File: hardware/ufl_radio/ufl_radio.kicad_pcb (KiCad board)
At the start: 6 copper layers, 46.8 x 62 mm, 142 parts, among them J2 U.FL, J3 Shield, J4 Shield, J5 U.FL, J6 Shield, J7 U.FL, J8 Shield, J9 U.FL, U1 MAX2769B, U2 CS48520S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

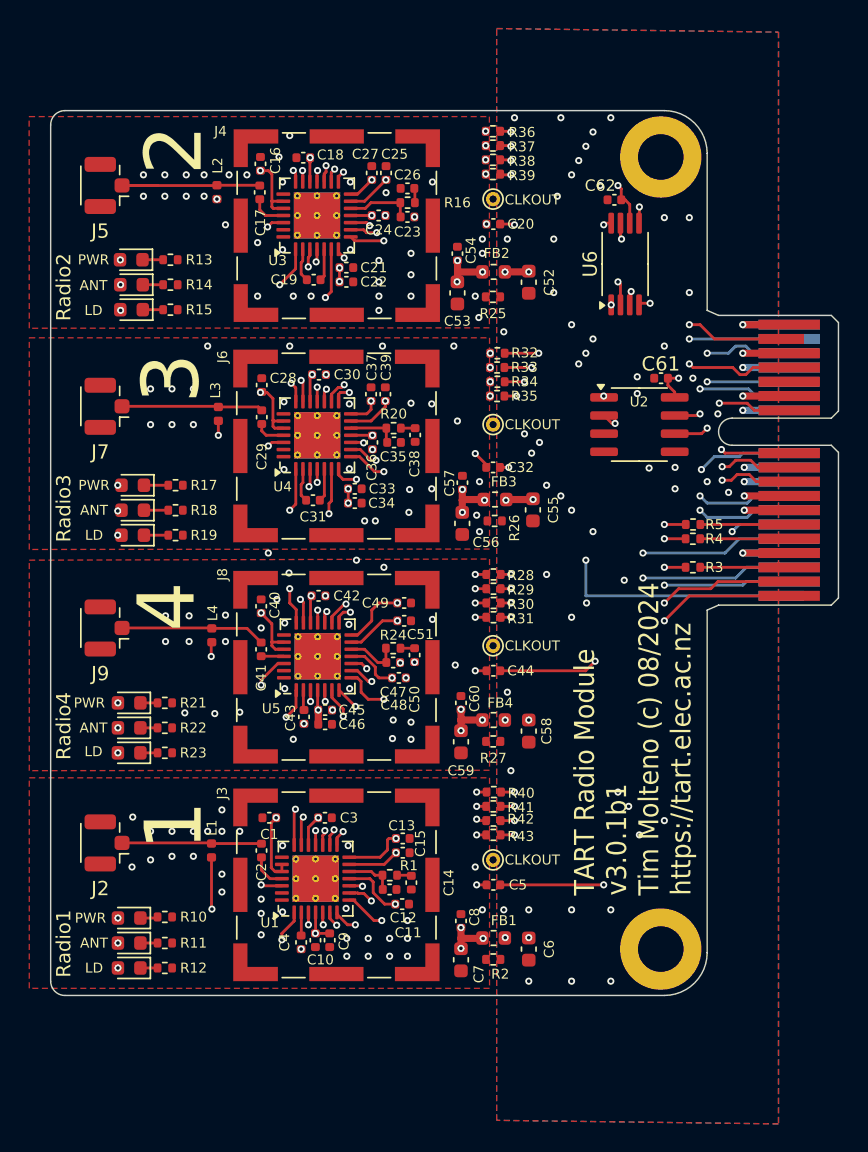
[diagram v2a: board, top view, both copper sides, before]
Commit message: Updated the order of radios
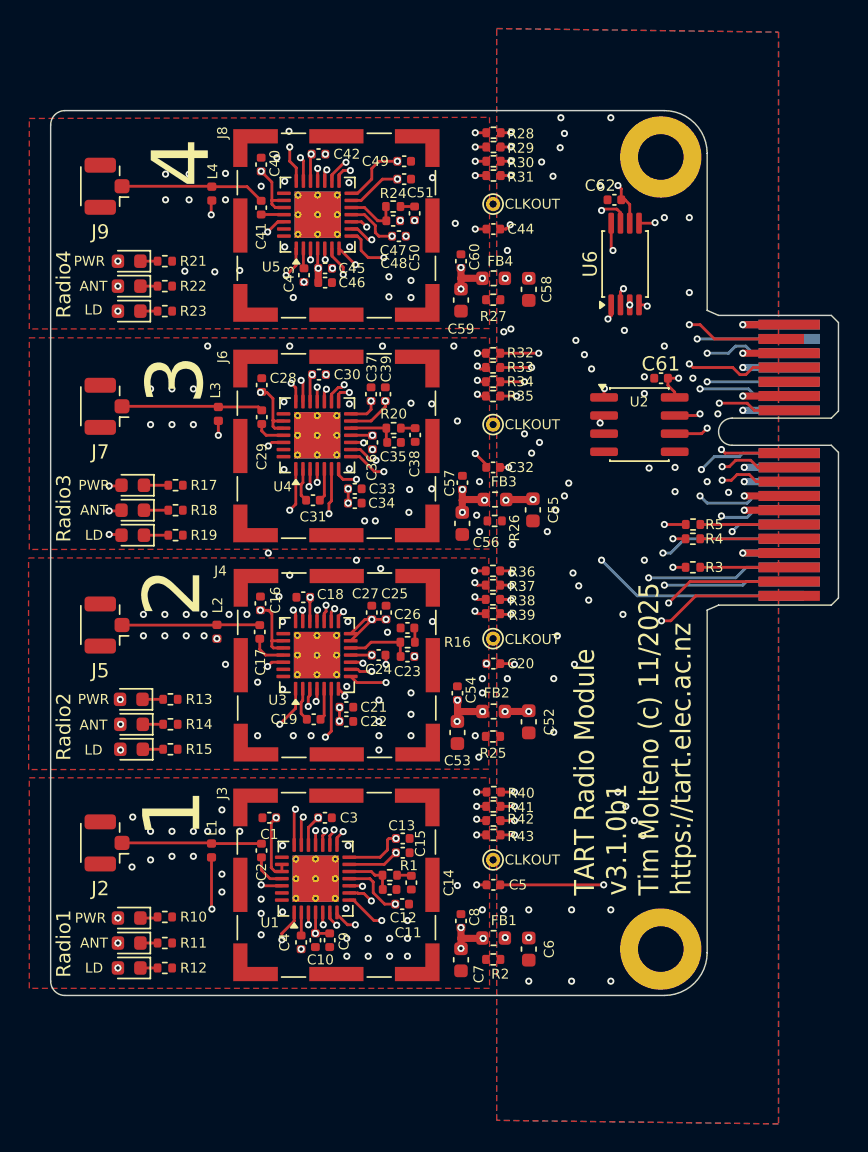
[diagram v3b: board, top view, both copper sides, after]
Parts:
- moved C40 31.0 mm to (174.8, 77.8)
- moved C41 31.0 mm to (174.8, 80.8)
- moved C42 31.0 mm to (178.8, 77.0)
- moved C43 31.0 mm to (177.8, 85.5)
- moved C44 31.0 mm to (191.0, 82.3)
- moved C45 31.0 mm to (179.2, 85.0)
- moved C46 31.0 mm to (179.2, 86.0)
- moved C47 31.0 mm to (184.0, 81.7)
- moved C48 31.0 mm to (184.4, 82.8)
- moved C49 31.0 mm to (184.8, 77.5)
- moved C50 31.0 mm to (185.5, 81.2)
- moved C51 31.0 mm to (184.8, 78.8)
- moved C60 31.0 mm to (188.8, 84.5)
- moved D10 31.0 mm to (165.5, 84.5)
- moved D11 31.0 mm to (165.5, 86.3)
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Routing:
- net CLKIN_2: track 7.84 -> 37.5 mm, vias 2 -> 3
- net CLKIN_4: track 38.7 -> 9.85 mm
- net R4_Q0: track 25.2 -> 46.1 mm
- net R4_I0: track 26.7 -> 45.0 mm, vias 3 -> 4
- net R4_I1: track 27.4 -> 45.4 mm
- net R4_Q1: track 28.1 -> 43.9 mm
- net R2_Q1: track 30.6 -> 40.1 mm
- net Net-(J5-In): track 12.2 -> 9.67 mm
- net R2_Q0: track 35.0 -> 37.0 mm
- net R2_I1: track 34.8 -> 36.5 mm
- net CLKIN_1: track 50.6 -> 49.0 mm
- net CLKIN_3: track 30.7 -> 29.1 mm
- net R2_I0: track 35.2 -> 36.7 mm
- net /Radio3/LD: track 18.6 -> 20.1 mm
- net /Radio3/ANTFLAG: track 15.1 -> 16.6 mm
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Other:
- board text added: "TART Radio Module v3.1.0b1 Tim Molteno (c) 11/2025 https://tart.elec.ac.nz"
- board text added: "TART Radio Telescope Radio Module v3.1.0b1 Tim Molteno (c) 11/2025 https://tart.elec.ac.nz"
- board text removed: "TART Radio Module v3.0.1b1 Tim Molteno (c) 08/2024 https://tart.elec.ac.nz"
- board text removed: "TART Radio Telescope Radio Module v3.0.1b1 Tim Molteno (c) 08/2024 https://tart.elec.ac.nz"

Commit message: Minor updates
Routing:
- net GNDREF: track 30.4 -> 29.8 mm
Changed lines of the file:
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@@
-	)
-	(segment
-		(start 198.775 95.365)
-		(end 198.5 95.64)
-		(width 0.2)
-		(layer "F.Cu")
-		(net 27)
 	)
 	(segment
@@
 		(end 211.75 89)
 		(width 0.5)
-		(layer "F.Cu")
-		(net 27)
-	)
-	(segment
-		(start 198.5 95.64)
-		(end 198.5 95.887475)
-		(width 0.2)
 		(layer "F.Cu")
 		(net 27)
@@
 	)
 	(via
-		(at 198.5 95.887475)
-		(size 0.5)
-		(drill 0.25)
+		(at 201.7 95.5)
+		(size 0.5)
+		(drill 0.25)

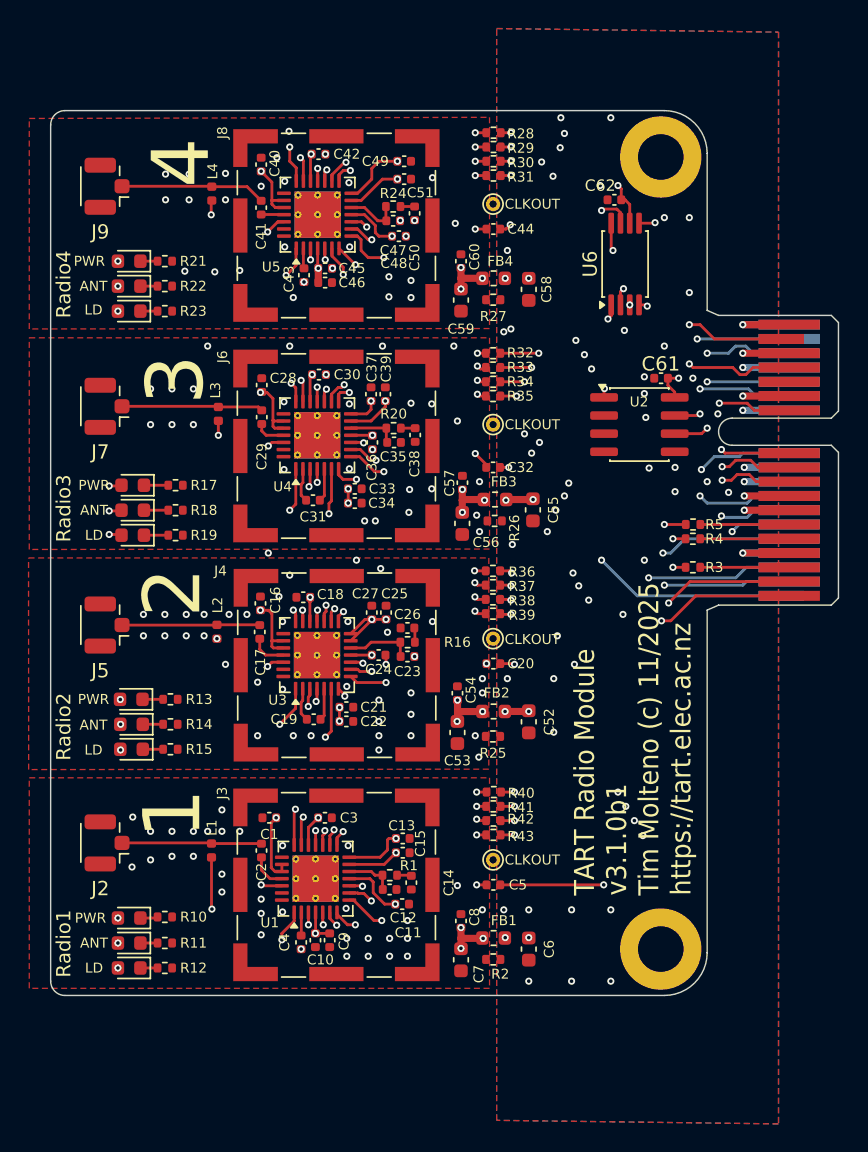
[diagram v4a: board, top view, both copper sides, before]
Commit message: Added radio board with identical sections
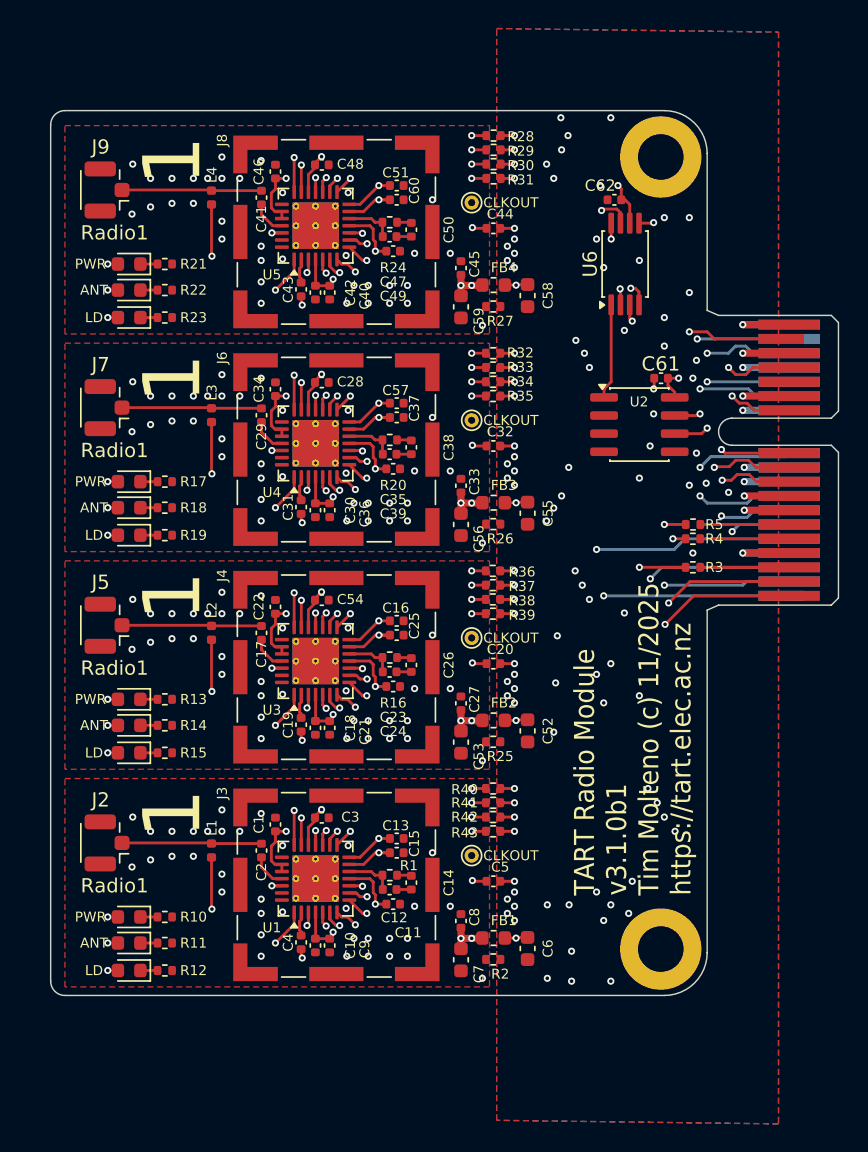
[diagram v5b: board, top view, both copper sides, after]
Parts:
- moved C54 11.5 mm to (179.0, 108.3), turned to 0 degrees
- moved C40 10.2 mm to (179.6, 86.8), turned to -90 degrees
- moved C34 9.73 mm to (175.8, 93.5), turned to 90 degrees
- moved C42 9.70 mm to (178.6, 86.8), turned to -90 degrees
- moved C16 9.63 mm to (184.2, 109.8), turned to 0 degrees
- moved C45 9.52 mm to (188.8, 85.0), turned to 90 degrees
- moved C30 9.50 mm to (178.6, 102.0), turned to -90 degrees
- moved C22 9.44 mm to (175.8, 108.8), turned to 90 degrees
- moved C18 9.19 mm to (178.6, 117.2), turned to -90 degrees
- moved C27 8.92 mm to (188.8, 115.5)
- moved C46 8.52 mm to (175.8, 78.3), turned to 90 degrees
- moved C33 7.44 mm to (188.8, 100.3), turned to 90 degrees
- moved C48 7.36 mm to (179.0, 77.8)
- moved C57 7.22 mm to (184.2, 94.5), turned to 0 degrees
- moved C49 6.35 mm to (184.0, 83.8)
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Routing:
- net PGM: track 88.3 -> 156.0 mm, vias 6 -> 12
- net /SHDN: track 84.0 -> 134.9 mm, vias 6 -> 12
- net SDATA: track 81.9 -> 131.4 mm, vias 6 -> 13
- net SCLK: track 76.9 -> 49.6 mm, vias 6 -> 9
- net CS#: track 73.6 -> 46.7 mm, vias 6 -> 9
- net R3_I0: track 27.4 -> 6.06 mm, vias 3 -> 2
- net R3_I1: track 27.6 -> 6.65 mm, vias 3 -> 2
- net R3_Q0: track 24.4 -> 5.84 mm, vias 3 -> 2
- net /Radio2/3v3_local: track 18.1 -> 25.8 mm, vias 12 -> 9
- net /Radio3/3v3_local: track 19.3 -> 25.8 mm, vias 12 -> 9
- net VCC: track 19.7 -> 22.5 mm, vias 14 -> 10
- net /Radio2/LD: track 18.3 -> 20.7 mm
- net Net-(U3-MIXIN): track 2.24 -> 4.64 mm, vias 0 -> 2
- net Net-(U4-MIXIN): track 2.32 -> 4.64 mm, vias 0 -> 2
- net Net-(U4-XTAL): track 14.4 -> 12.3 mm
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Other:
- board text removed: "2"
- board text removed: "3"
- board text removed: "4"
- board text removed: "Radio2"
- board text removed: "Radio3"
- board text removed: "Radio4"

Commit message: DRC passing mostly
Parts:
- moved C48 12.1 mm to (188.8, 85.0), turned to 90 degrees
- moved C54 12.1 mm to (188.8, 115.5), turned to 90 degrees
- moved C39 9.96 mm to (175.8, 93.5), turned to 90 degrees
- moved C18 9.42 mm to (184.2, 109.8), turned to 0 degrees
- moved C51 9.42 mm to (178.6, 86.8), turned to -90 degrees
- moved C27 9.36 mm to (179.6, 117.2), turned to -90 degrees
- moved C22 8.93 mm to (178.6, 117.2), turned to -90 degrees
- moved C42 8.93 mm to (175.8, 78.3), turned to 90 degrees
- moved C25 8.73 mm to (175.8, 108.8), turned to 90 degrees
- moved C46 8.73 mm to (184.2, 80.2), turned to 0 degrees
- moved C28 7.85 mm to (184.0, 99.1)
- moved C45 7.33 mm to (184.2, 79.2), turned to 0 degrees
- moved C33 6.56 mm to (184.2, 95.5), turned to 0 degrees
- moved C37 6.56 mm to (188.8, 100.3), turned to 90 degrees
- moved C60 5.79 mm to (179.0, 77.8)
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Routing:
- net CS#: track 46.7 -> 130.2 mm
- net SCLK: track 49.6 -> 128.9 mm, vias 9 -> 10
- net R3_I0: track 6.06 -> 28.8 mm, vias 2 -> 4
- net R3_I1: track 6.65 -> 29.0 mm, vias 2 -> 4
- net R3_Q0: track 5.84 -> 24.2 mm, vias 2 -> 3
- net R4_I1: track 43.9 -> 42.2 mm
- net SDATA: track 131.4 -> 133.0 mm, vias 13 -> 9
- net CLKIN_1: track 49.7 -> 50.9 mm
- net GNDREF: track 31.5 -> 30.4 mm
- net CLKIN_2: track 38.6 -> 39.4 mm
- net /SHDN: track 134.9 -> 135.3 mm, vias 12 -> 9
- net PGM: track 156.0 -> 156.3 mm, vias 12 -> 9
